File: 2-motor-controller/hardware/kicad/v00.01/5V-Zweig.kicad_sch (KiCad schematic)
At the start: 7 parts, among them U101 R-78B5.0-2.0

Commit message: Motor-Controller: Hauptblatt nach Zweck gegliedert, Blatt Endstufe, eigene Bibliothek; Bauteilauswahl 00.20 / Stueckliste 00.16; 99-tools angelegt
Co-Authored-By: Claude Opus 5.5 <noreply@anthropic.com>
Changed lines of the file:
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@@
+	)
+	(symbol
+		(lib_id "power:PWR_FLAG")
+		(at 93.98 76.2 0)
+		(unit 1)
+		(body_style 1)
+		(exclude_from_sim no)
+		(in_bom yes)
+		(on_board yes)
+		(in_pos_files yes)
+		(dnp no)
+		(property "Reference" "#FLG101"
+			(at 93.98 73.66 0)
+			(hide yes)
+			(show_name no)
+			(do_not_autoplace no)
+			(effects
+				(font
+					(size 1.27 1.27)
+				)
+			)
+		)
+		(property "Value" "PWR_FLAG"
+			(at 93.98 78.74 0)
+			(hide yes)
+			(show_name no)
+			(do_not_autoplace no)
+			(effects
+				(font
+					(size 1.27 1.27)
+				)
+			)
+		)
+		(property "Footprint" ""
+			(at 93.98 76.2 0)
+			(hide yes)
+			(show_name no)
+			(do_not_autoplace no)
+			(effects
+				(font
+					(size 1.27 1.27)
+				)
+			)
+		)
+		(property "Datasheet" ""
+			(at 93.98 76.2 0)
+			(hide yes)
+			(show_name no)
+			(do_not_autoplace no)
+			(effects
+				(font
+					(size 1.27 1.27)
+				)
+			)
+		)
+		(property "Description" "Special symbol for telling ERC where power comes from"
+			(at 93.98 76.2 0)
+			(hide yes)
+			(show_name no)
+			(do_not_autoplace no)
+			(effects
+				(font
+					(size 1.27 1.27)
+				)
+			)
+		)
+		(pin "1"
+		)
+		(instances
+			(project "Motor-Controller"
+				(path "/255b263c-8a60-4b67-92ab-70f539cf8eaf/308cdea6-e3ed-4042-bab9-d5931def5bc5"
+					(reference "#FLG101")
+					(unit 1)
+				)
+				(path "/255b263c-8a60-4b67-92ab-70f539cf8eaf/6e08cac9-0d96-4a68-acc9-44be3610c2a8"
+					(reference "#FLG4")
+					(unit 1)
+				)
+			)
+		)
 	)
 	(symbol

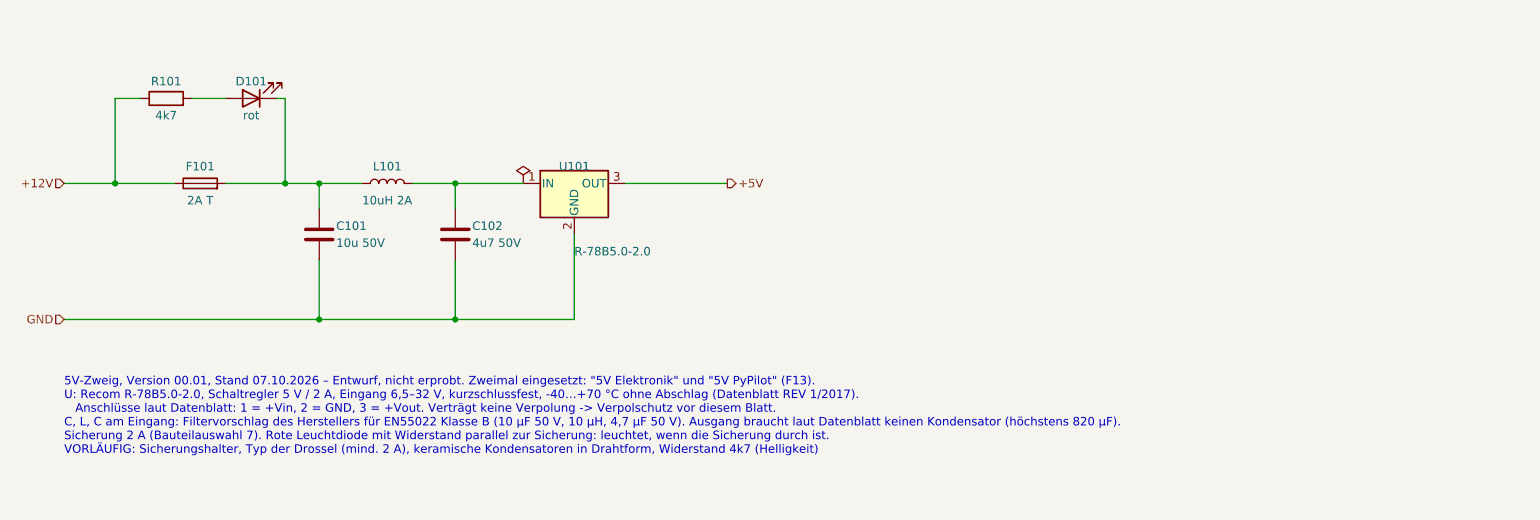
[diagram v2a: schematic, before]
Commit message: Motor-Controller: alle Blaetter nach den Zeichenregeln (Rahmen, Gruppen), 5-V-Zweig mit 2 x 4,7 uF, Titelfelder Version 00.01; Pruefung gegen Blockschaltbild 78/78
Co-Authored-By: Claude Opus 5.5 <noreply@anthropic.com>
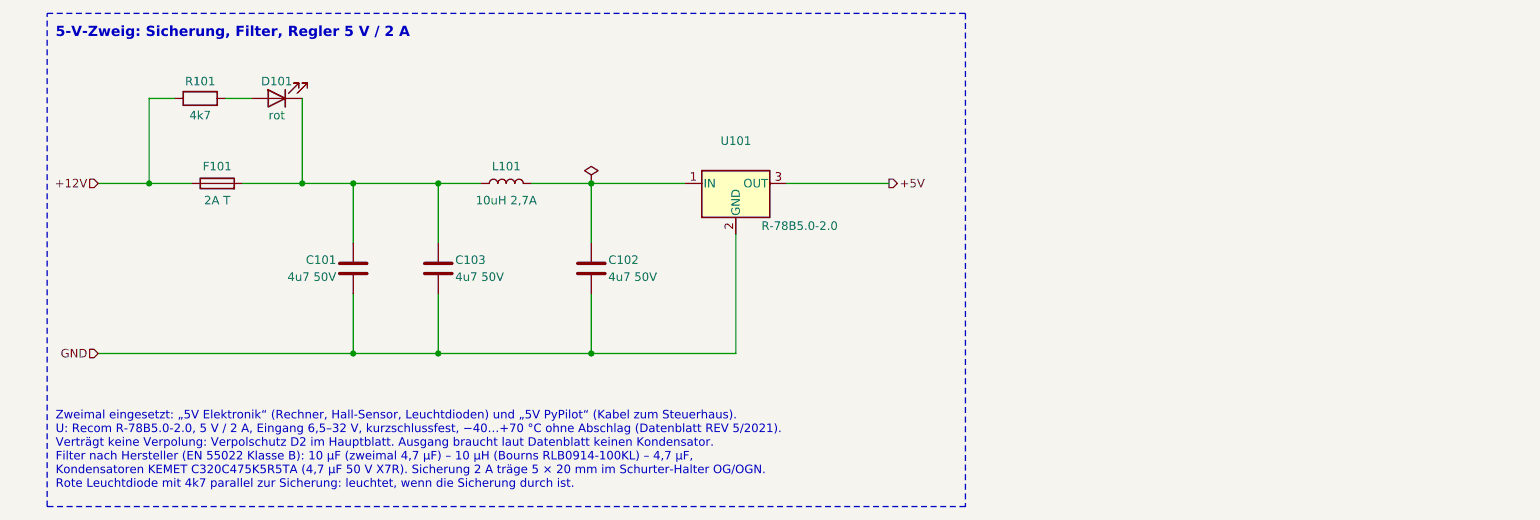
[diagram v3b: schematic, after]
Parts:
- added C103: 4u7 50V, Capacitor_THT:C_Disc_D7.5mm_W5.0mm_P5.00mm, symbol Device:C
- C101: value 10u 50V -> 4u7 50V
- L101: value 10uH 2A -> 10uH 2,7A
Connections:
- net GND: now also C103.2
- net at C101.1, D101.1 (K), F101.2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: now also C103.1
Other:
- note added: "5-V-Zweig: Sicherung, Filter, Regler 5 V / 2 A"
- note added: "Zweimal eingesetzt: „5V Elektronik“ (Rechner, Hall-Sensor, Leuchtdioden) und „5V PyPilot“ (Kabel zum Steuerhaus). U: Recom R-78B5.0-2.0, 5 V / 2 A, Eingang 6,5–32 V, kurzschlussfest, −40…+70 °C ohne Abschlag (Datenblatt REV 5/2021). Verträgt keine Verpolung: Verpolschutz D2 im Hauptblatt. Ausgang braucht laut Datenblatt keinen Kondensator. Filter nach Hersteller (EN 55022 Klasse B): 10 µF (zweima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"
- note removed: "5V-Zweig, Version 00.01, Stand 07.10.2026 – Entwurf, nicht erprobt. Zweimal eingesetzt: "5V Elektronik" und "5V PyPilot" (F13). U: Recom R-78B5.0-2.0, Schaltregler 5 V / 2 A, Eingang 6,5–32 V, kurzschlussfest, -40…+70 °C ohne Abschlag (Datenblatt REV 1/2017). Anschlüsse laut Datenblatt: 1 = +Vin, 2 = GND, 3 = +Vout. Verträgt keine Verpolung -> Verpolschutz vor diesem Blatt. C, L, C am Eingang: Fi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"
- company: (none) -> SuAn-Autopilot-Projekt
- title: (none) -> Motor-Controller V2.0 – 5-V-Zweig

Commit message: Motor-Controller: Loetbilder zugeordnet (eigene: Dialight 551, TL1105, KEMET C320, Display-Leiste), Platine 150 x 130 mm mit allen 94 Teilen angeordnet - Bauteilauswahl 00.23, Anforderungen 00.11, Stueckliste 00.19
Co-Authored-By: Claude Opus 5.5 <noreply@anthropic.com>
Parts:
- C101, C102, C103: footprint Capacitor_THT:C_Disc_D7.5mm_W5.0mm_P5.00mm -> Motor-Controller:C_KEMET_C320_L5.1mm_W4.1mm_P2.54mm
- D101: footprint LED_THT:LED_D3.0mm -> Motor-Controller:LED_Dialight_551_RightAngle
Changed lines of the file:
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@@
 			)
 		)
-		(property "Footprint" "LED_THT:LED_D3.0mm"
+		(property "Footprint" "Motor-Controller:LED_Dialight_551_RightAngle"
 			(at 57.15 63.5 0)
 			(hide yes)
@@
 			)
 		)
-		(property "Footprint" "Capacitor_THT:C_Disc_D7.5mm_W5.0mm_P5.00mm"
+		(property "Footprint" "Motor-Controller:C_KEMET_C320_L5.1mm_W4.1mm_P2.54mm"
 			(at 68.58 88.9 0)
 			(hide yes)
@@
 			)
 		)
-		(property "Footprint" "Capacitor_THT:C_Disc_D7.5mm_W5.0mm_P5.00mm"
+		(property "Footprint" "Motor-Controller:C_KEMET_C320_L5.1mm_W4.1mm_P2.54mm"
 			(at 81.28 88.9 0)
 			(hide yes)
@@
 			)
 		)
-		(property "Footprint" "Capacitor_THT:C_Disc_D7.5mm_W5.0mm_P5.00mm"
+		(property "Footprint" "Motor-Controller:C_KEMET_C320_L5.1mm_W4.1mm_P2.54mm"
 			(at 104.14 88.9 0)
 			(hide yes)

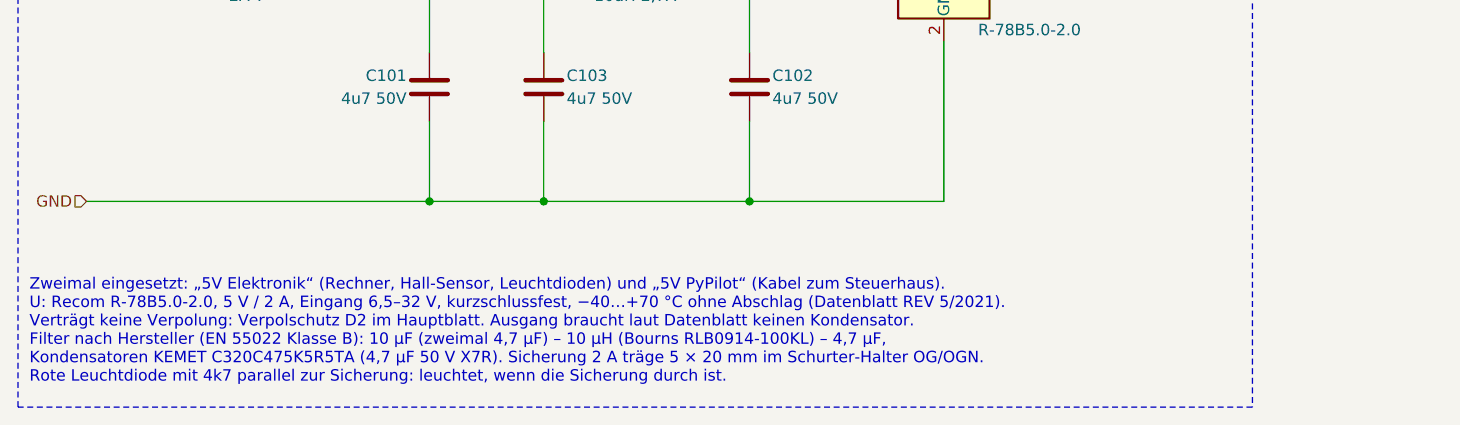
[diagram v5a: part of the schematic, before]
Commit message: 12 V zum Steuerstand statt 5 V: eigener Regler 12->5 V (3 A) am Steuerstand
Vom Motorraum gehen 12 V (rot/schwarz) zum Regler am Steuerstand, von dort 5 V
(zweites rot/schwarzes Paar) zur PyPilot-Einheit.
- Systembeschreibung, TODO (Frage 1 geloescht, Frage 18 gekuerzt)
- Motor-Controller: F13 (motorcontroller 00.13), Bauteilauswahl 00.26,
  Blockschaltbild 00.07, Stueckliste 00.21: J7.8 = +12 V hinter D2, ohne
  eigene Sicherung (Betreiber 13.10.2026); zweiter 5-V-Zweig entfernt
- KiCad v00.01: Blatt "5V PyPilot" und 8 Bauteile entfernt; ERC 0 Fehler,
  Paritaet 0, pruefung_blockschaltbild 00.03: 78/78
- Phase 1 Verdrahtungsplaene: Basic (Regler vor TinyPilot), Dual Display
  (Masse zum Regler); Vermerk Einbauort

Co-Authored-By: Claude Opus 5.5 <noreply@anthropic.com>
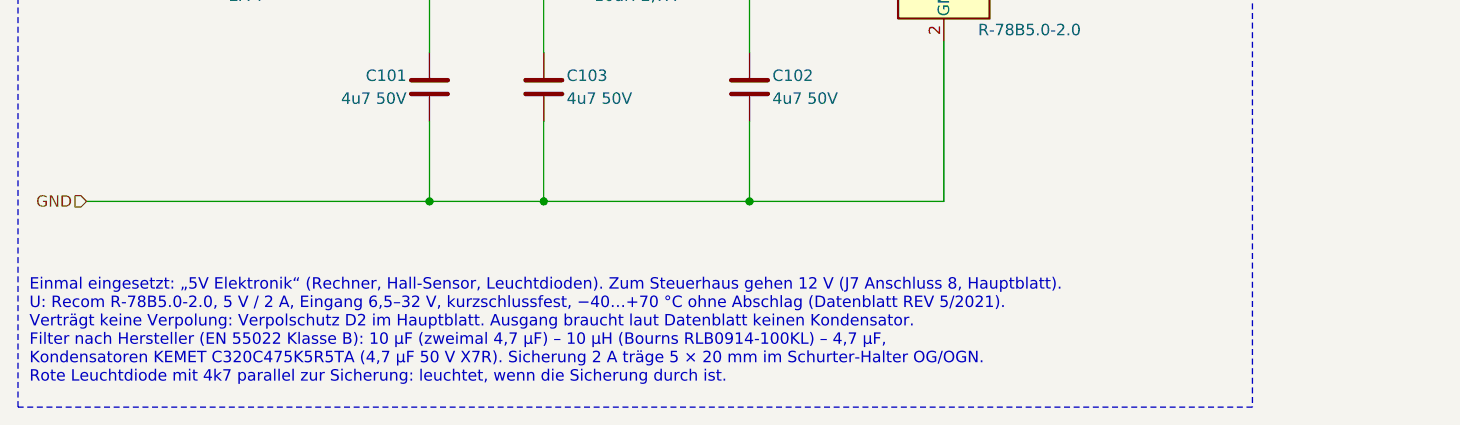
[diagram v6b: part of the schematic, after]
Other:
- note added: "Einmal eingesetzt: „5V Elektronik“ (Rechner, Hall-Sensor, Leuchtdioden). Zum Steuerhaus gehen 12 V (J7 Anschluss 8, Hauptblatt). U: Recom R-78B5.0-2.0, 5 V / 2 A, Eingang 6,5–32 V, kurzschlussfest, −40…+70 °C ohne Abschlag (Datenblatt REV 5/2021). Verträgt keine Verpolung: Verpolschutz D2 im Hauptblatt. Ausgang braucht laut Datenblatt keinen Kondensator. Filter nach Hersteller (EN 55022 Klasse B)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"
- note removed: "Zweimal eingesetzt: „5V Elektronik“ (Rechner, Hall-Sensor, Leuchtdioden) und „5V PyPilot“ (Kabel zum Steuerhaus). U: Recom R-78B5.0-2.0, 5 V / 2 A, Eingang 6,5–32 V, kurzschlussfest, −40…+70 °C ohne Abschlag (Datenblatt REV 5/2021). Verträgt keine Verpolung: Verpolschutz D2 im Hauptblatt. Ausgang braucht laut Datenblatt keinen Kondensator. Filter nach Hersteller (EN 55022 Klasse B): 10 µF (zweima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"
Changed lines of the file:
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@@
 		)
 	)
-	(text "Zweimal eingesetzt: „5V Elektronik“ (Rechner, Hall-Sensor, Leuchtdioden) und „5V PyPilot“ (Kabel zum Steuerhaus).\nU: Recom R-78B5.0-2.0, 5 V / 2 A, Eingang 6,5–32 V, kurzschlussfest, −40…+70 °C ohne Abschlag (Datenblatt REV 5/2021).\nVerträgt keine Verpolung: Verpolschutz D2 im Hauptblatt. Ausgang braucht laut Datenblatt keinen Kondensator.\nFilter nach Hersteller (EN 55022 Klasse B): 10 µF (zweimal 4,7 µF) – 10 µH (Bourns RLB0914-100KL) – 4,7 µF,\nKondensatoren KEMET C320C475K5R5TA (4,7 µF 50 V X7R). Sicherung 2 A träge 5 × 20 mm im Schurter-Halter OG/OGN.\nRote Leuchtdiode mit 4k7 parallel zur Sicherung: leuchtet, wenn die Sicherung durch ist."
+	(text "Einmal eingesetzt: „5V Elektronik“ (Rechner, Hall-Sensor, Leuchtdioden). Zum Steuerhaus gehen 12 V (J7 Anschluss 8, Hauptblatt).\nU: Recom R-78B5.0-2.0, 5 V / 2 A, Eingang 6,5–32 V, kurzschlussfest, −40…+70 °C ohne Abschlag (Datenblatt REV 5/2021).\nVerträgt keine Verpolung: Verpolschutz D2 im Hauptblatt. Ausgang braucht laut Datenblatt keinen Kondensator.\nFilter nach Hersteller (EN 55022 Klasse B): 10 µF (zweimal 4,7 µF) – 10 µH (Bourns RLB0914-100KL) – 4,7 µF,\nKondensatoren KEMET C320C475K5R5TA (4,7 µF 50 V X7R). Sicherung 2 A träge 5 × 20 mm im Schurter-Halter OG/OGN.\nRote Leuchtdiode mit 4k7 parallel zur Sicherung: leuchtet, wenn die Sicherung durch ist."
 		(exclude_from_sim no)
 		(at 24.13 121.92 0)
@@
 					(unit 1)
 				)
-				(path "/255b263c-8a60-4b67-92ab-70f539cf8eaf/6e08cac9-0d96-4a68-acc9-44be3610c2a8"
-					(reference "F201")
-					(unit 1)
-				)
 			)
 		)
@@
 					(unit 1)
 				)
-				(path "/255b263c-8a60-4b67-92ab-70f539cf8eaf/6e08cac9-0d96-4a68-acc9-44be3610c2a8"
-					(reference "U201")
-					(unit 1)
-				)
 			)
 		)
@@
 					(unit 1)
 				)
-				(path "/255b263c-8a60-4b67-92ab-70f539cf8eaf/6e08cac9-0d96-4a68-acc9-44be3610c2a8"
-					(reference "L201")
-					(unit 1)
-				)
 			)
 		)
@@
 					(unit 1)
 				)
-				(path "/255b263c-8a60-4b67-92ab-70f539cf8eaf/6e08cac9-0d96-4a68-acc9-44be3610c2a8"
-					(reference "D201")
-					(unit 1)
-				)
 			)
 		)
@@
 					(unit 1)
 				)
-				(path "/255b263c-8a60-4b67-92ab-70f539cf8eaf/6e08cac9-0d96-4a68-acc9-44be3610c2a8"
-					(reference "C201")
-					(unit 1)
-				)
 			)
 		)
@@
 					(unit 1)
 				)
-				(path "/255b263c-8a60-4b67-92ab-70f539cf8eaf/6e08cac9-0d96-4a68-acc9-44be3610c2a8"
-					(reference "C203")
-					(unit 1)
-				)
 			)
 		)
@@
 					(unit 1)
 				)
-				(path "/255b263c-8a60-4b67-92ab-70f539cf8eaf/6e08cac9-0d96-4a68-acc9-44be3610c2a8"
-					(reference "C202")
-					(unit 1)
-				)
 			)
 		)
@@
 					(unit 1)
 				)
-				(path "/255b263c-8a60-4b67-92ab-70f539cf8eaf/6e08cac9-0d96-4a68-acc9-44be3610c2a8"
-					(reference "#FLG201")
-					(unit 1)
-				)
 			)
 		)
@@
 					(unit 1)
 				)
-				(path "/255b263c-8a60-4b67-92ab-70f539cf8eaf/6e08cac9-0d96-4a68-acc9-44be3610c2a8"
-					(reference "R201")
-					(unit 1)
-				)
-			)
-		)
-	)
-	(sheet_instances
-		(path "/"
-			(page "1")
-		)
-	)
+			)
+		)
+	)
